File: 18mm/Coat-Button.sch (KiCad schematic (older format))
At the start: 25 parts, among them IC1 MADW__ATTINY13-MM, P1 CONN_1, P2 CONN_1, P3 CONN_1, P4 CONN_1

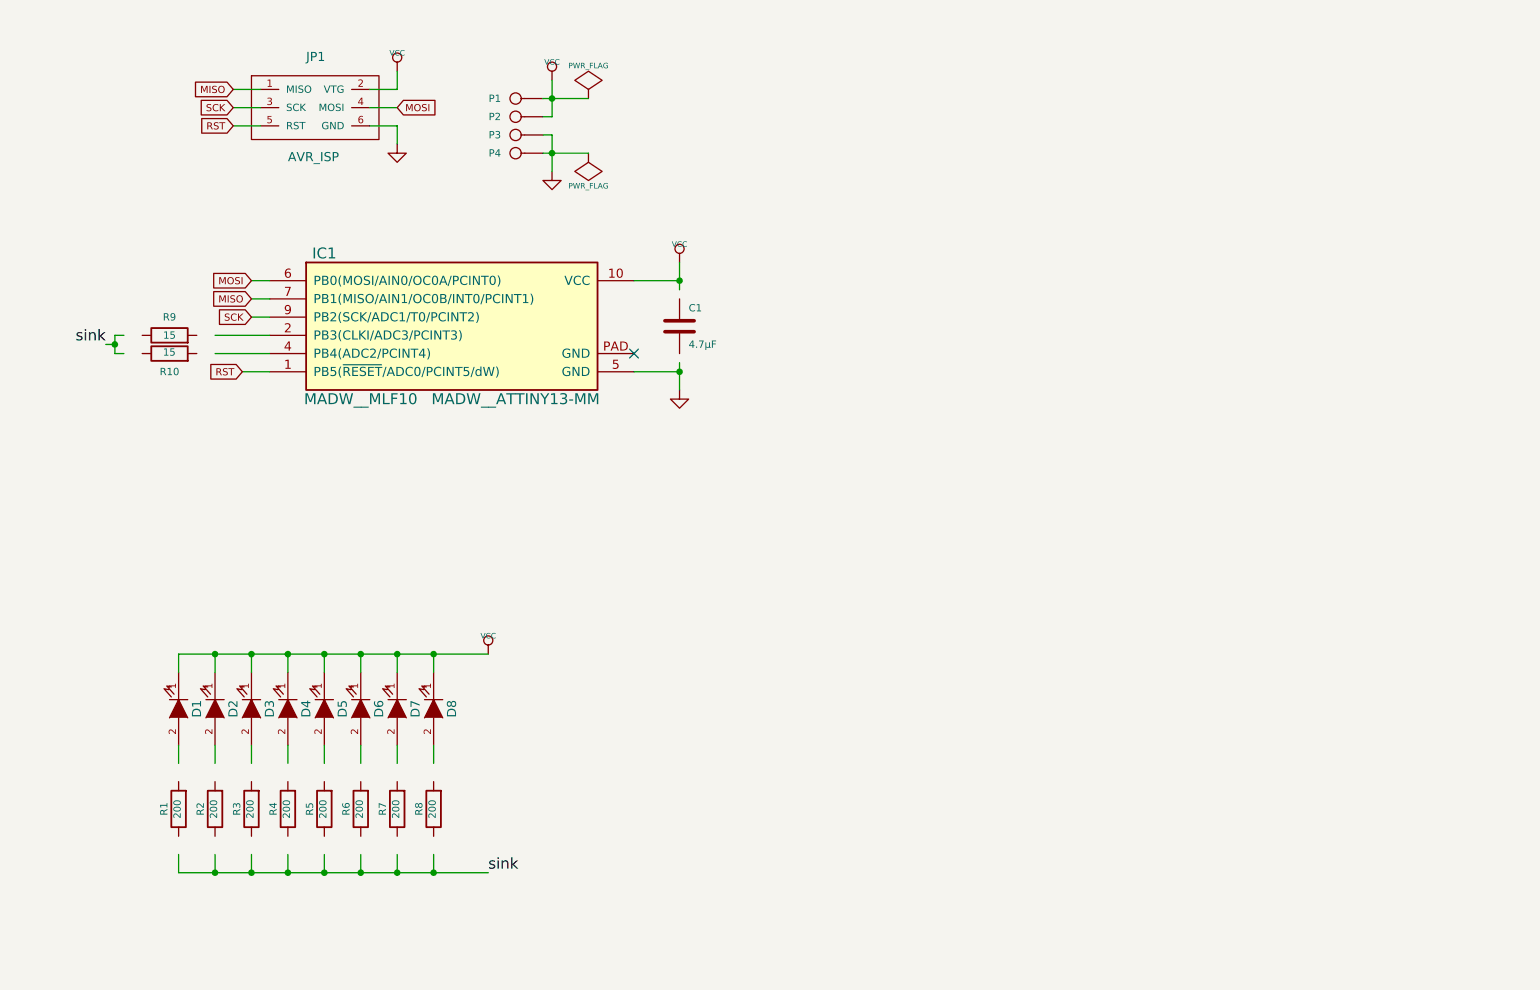
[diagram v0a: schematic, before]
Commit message: Made one with dual-colour LEDs (0805). Just to see if possible.
Had to use 0402 resitors...
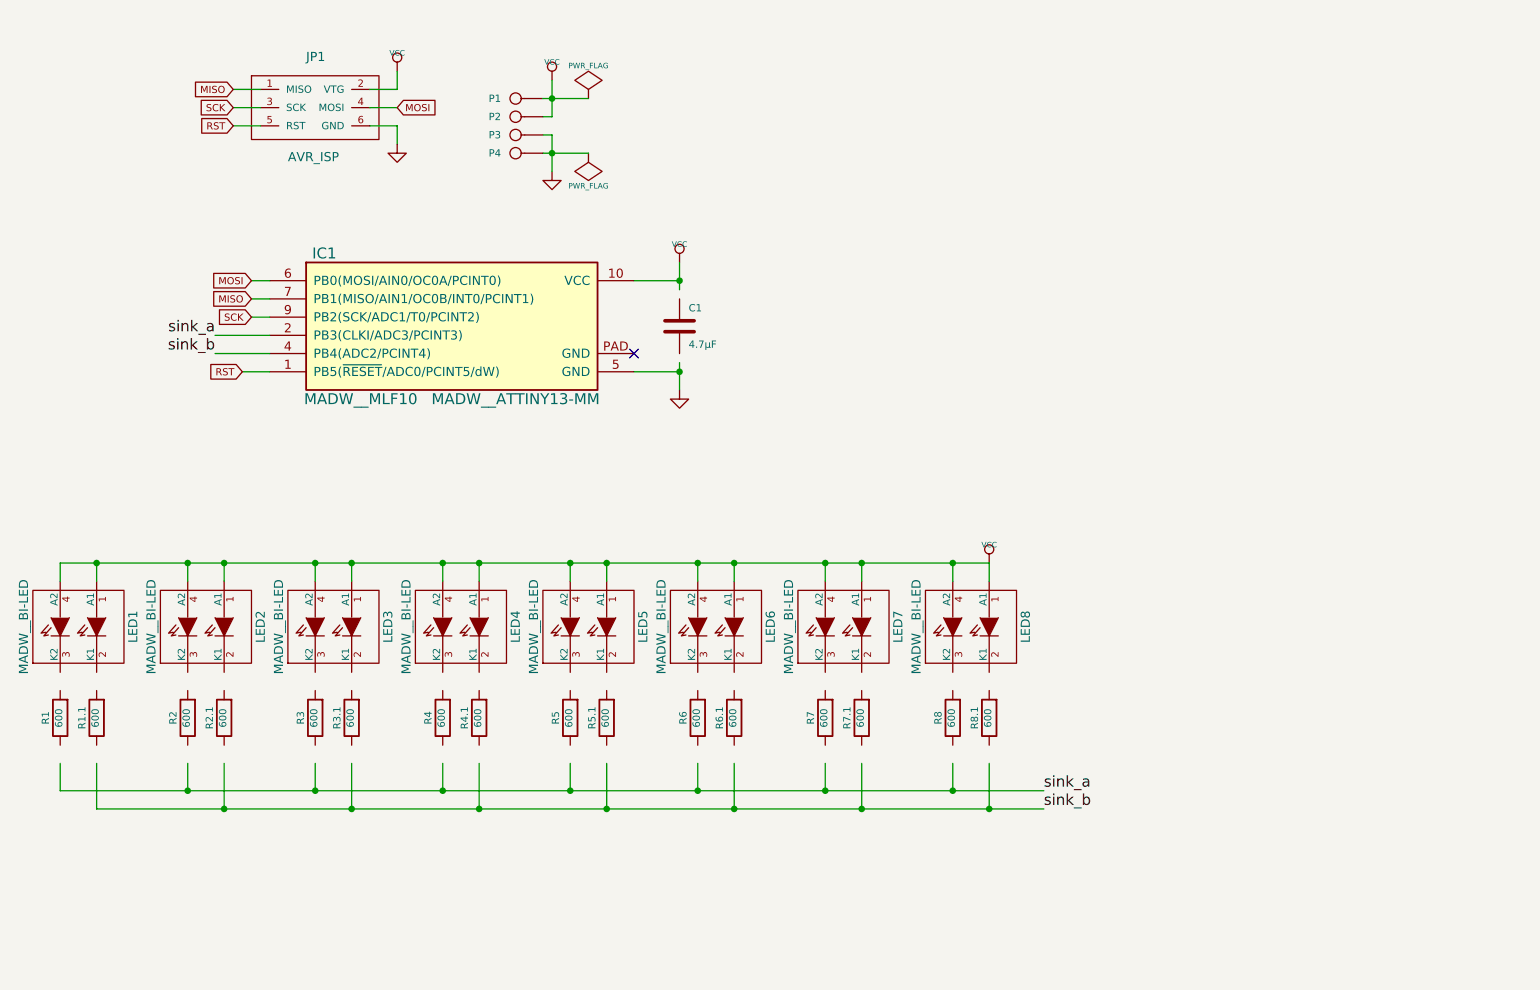
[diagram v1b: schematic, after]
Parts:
- removed D1, D2, D3, D4, D5, D6, D7, D8: LED, symbol LED
- removed R10, R9: 15, symbol R
- added LED1, LED2, LED3, LED4, LED5, LED6, LED7, LED8: MADW__BI-LED, symbol MADW__BI-LED
- added R1.1, R2.1, R3.1, R4.1, R5.1, R6.1, R7.1, R8.1: 600, symbol R
- R1, R2, R3, R4, R5, R6, R7, R8: value 200 -> 600
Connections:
- net labels added: sink_a, sink_b
- net labels removed: sink
- wire segments 54 -> 59
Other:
- moved on the sheet: R1, R2, R3, R4, R5, R6, R7, R8

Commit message: Added 2 SOT523 n-ch mosfets + reduced LED resistors.
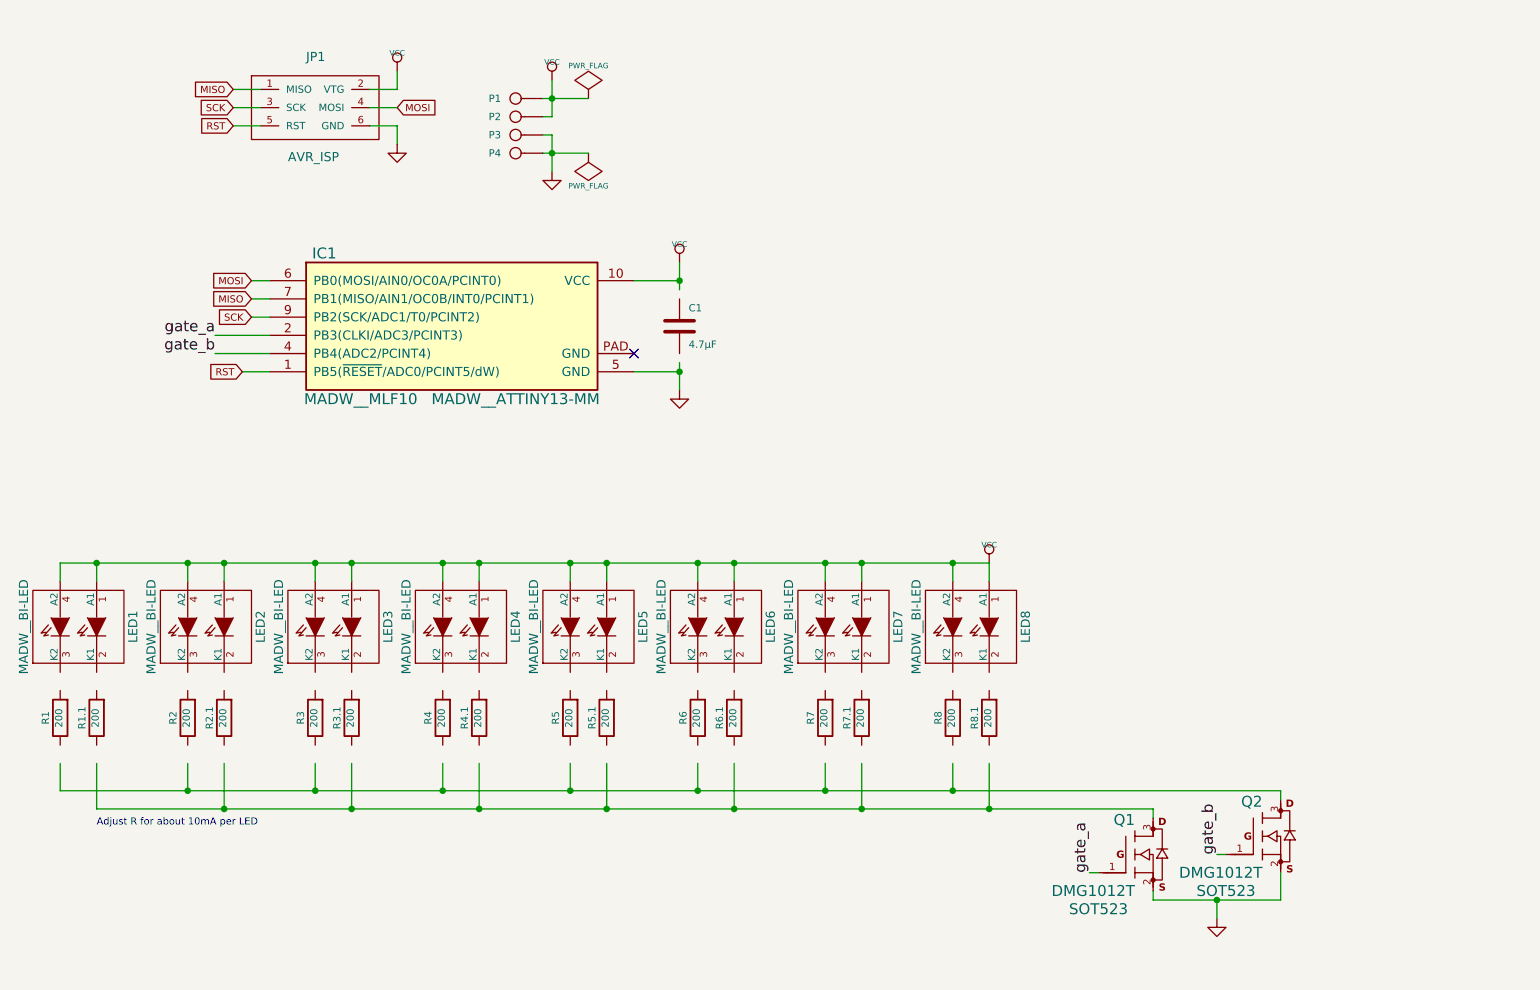
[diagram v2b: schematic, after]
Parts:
- added Q1, Q2: DMG1012T, SOT523, symbol MOSFET_N
- R1, R1.1, R2, R2.1, R3, R3.1, R4, R4.1, R5, R5.1, R6, R6.1, R7, R7.1, R8, R8.1: value 600 -> 200
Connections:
- net labels added: gate_a, gate_b
- net labels removed: sink_a, sink_b
- wire segments 59 -> 67
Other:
- note added: "Adjust R for about 10mA per LED"
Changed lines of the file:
@@
 EESchema Schematic File Version 2
+LIBS:my_parts
 LIBS:power
 LIBS:device
@@
 LIBS:contrib
 LIBS:valves
-LIBS:my_parts
 LIBS:Coat-Button-cache
 EELAYER 24 0
@@
 Sheet 1 1
 Title "Coat-Button"
-Date "23 Sep 2013"
-Rev "0.2"
+Date "25 Sep 2013"
+Rev "0.21"
 Comp "2013 - blog.spitzenpfeil.org"
 Comment1 ""
@@
 P 2300 5100
 F 0 "R1" V 2380 5100 40  0000 C CNN
-F 1 "600" V 2307 5101 40  0000 C CNN
+F 1 "200" V 2307 5101 40  0000 C CNN
 F 2 "" V 2230 5100 30  0000 C CNN
 F 3 "" H 2300 5100 30  0000 C CNN
@@
 P 3000 5100
 F 0 "R2" V 3080 5100 40  0000 C CNN
-F 1 "600" V 3007 5101 40  0000 C CNN
+F 1 "200" V 3007 5101 40  0000 C CNN
 F 2 "" V 2930 5100 30  0000 C CNN
 F 3 "" H 3000 5100 30  0000 C CNN
@@
 P 3700 5100
 F 0 "R3" V 3780 5100 40  0000 C CNN
-F 1 "600" V 3707 5101 40  0000 C CNN
+F 1 "200" V 3707 5101 40  0000 C CNN
 F 2 "" V 3630 5100 30  0000 C CNN
 F 3 "" H 3700 5100 30  0000 C CNN
@@
 P 4400 5100
 F 0 "R4" V 4480 5100 40  0000 C CNN
-F 1 "600" V 4407 5101 40  0000 C CNN
+F 1 "200" V 4407 5101 40  0000 C CNN
 F 2 "" V 4330 5100 30  0000 C CNN
 F 3 "" H 4400 5100 30  0000 C CNN
@@
 P 5100 5100
 F 0 "R5" V 5180 5100 40  0000 C CNN
-F 1 "600" V 5107 5101 40  0000 C CNN
+F 1 "200" V 5107 5101 40  0000 C CNN
 F 2 "" V 5030 5100 30  0000 C CNN
 F 3 "" H 5100 5100 30  0000 C CNN
@@
 P 5800 5100
 F 0 "R6" V 5880 5100 40  0000 C CNN
-F 1 "600" V 5807 5101 40  0000 C CNN
+F 1 "200" V 5807 5101 40  0000 C CNN
 F 2 "" V 5730 5100 30  0000 C CNN
 F 3 "" H 5800 5100 30  0000 C CNN
@@
 P 6500 5100
 F 0 "R7" V 6580 5100 40  0000 C CNN
-F 1 "600" V 6507 5101 40  0000 C CNN
+F 1 "200" V 6507 5101 40  0000 C CNN
 F 2 "" V 6430 5100 30  0000 C CNN
 F 3 "" H 6500 5100 30  0000 C CNN
@@
 P 7200 5100
 F 0 "R8" V 7280 5100 40  0000 C CNN
-F 1 "600" V 7207 5101 40  0000 C CNN
+F 1 "200" V 7207 5101 40  0000 C CNN
 F 2 "" V 7130 5100 30  0000 C CNN
 F 3 "" H 7200 5100 30  0000 C CNN
@@
 	3450 3100 3150 3100
 Text Label 3150 3000 2    60   ~ 0
-sink_a
-Text Label 7700 5500 0    60   ~ 0
-sink_a
+gate_a
 Wire Wire Line
 	4950 1900 5000 1900
@@
 P 2500 5100
 F 0 "R1.1" V 2580 5100 40  0000 C CNN
-F 1 "600" V 2507 5101 40  0000 C CNN
+F 1 "200" V 2507 5101 40  0000 C CNN
 F 2 "" V 2430 5100 30  0000 C CNN
 F 3 "" H 2500 5100 30  0000 C CNN
@@
 P 3200 5100
 F 0 "R2.1" V 3280 5100 40  0000 C CNN
-F 1 "600" V 3207 5101 40  0000 C CNN
+F 1 "200" V 3207 5101 40  0000 C CNN
 F 2 "" V 3130 5100 30  0000 C CNN
 F 3 "" H 3200 5100 30  0000 C CNN
@@
 P 3900 5100
 F 0 "R3.1" V 3980 5100 40  0000 C CNN
-F 1 "600" V 3907 5101 40  0000 C CNN
+F 1 "200" V 3907 5101 40  0000 C CNN
 F 2 "" V 3830 5100 30  0000 C CNN
 F 3 "" H 3900 5100 30  0000 C CNN
@@
 P 4600 5100
 F 0 "R4.1" V 4680 5100 40  0000 C CNN
-F 1 "600" V 4607 5101 40  0000 C CNN
+F 1 "200" V 4607 5101 40  0000 C CNN
 F 2 "" V 4530 5100 30  0000 C CNN
 F 3 "" H 4600 5100 30  0000 C CNN
@@
 P 5300 5100
 F 0 "R5.1" V 5380 5100 40  0000 C CNN
-F 1 "600" V 5307 5101 40  0000 C CNN
+F 1 "200" V 5307 5101 40  0000 C CNN
 F 2 "" V 5230 5100 30  0000 C CNN
 F 3 "" H 5300 5100 30  0000 C CNN
@@
 P 6000 5100
 F 0 "R6.1" V 6080 5100 40  0000 C CNN
-F 1 "600" V 6007 5101 40  0000 C CNN
+F 1 "200" V 6007 5101 40  0000 C CNN
 F 2 "" V 5930 5100 30  0000 C CNN
 F 3 "" H 6000 5100 30  0000 C CNN
@@
 P 6700 5100
 F 0 "R7.1" V 6780 5100 40  0000 C CNN
-F 1 "600" V 6707 5101 40  0000 C CNN
+F 1 "200" V 6707 5101 40  0000 C CNN
 F 2 "" V 6630 5100 30  0000 C CNN
 F 3 "" H 6700 5100 30  0000 C CNN
@@
 P 7400 5100
 F 0 "R8.1" V 7480 5100 40  0000 C CNN
-F 1 "600" V 7407 5101 40  0000 C CNN
+F 1 "200" V 7407 5101 40  0000 C CNN
 F 2 "" V 7330 5100 30  0000 C CNN
 F 3 "" H 7400 5100 30  0000 C CNN
@@
 	2300 5350 2300 5500
 Wire Wire Line
-	2300 5500 7700 5500
-Wire Wire Line
 	3000 5500 3000 5350
 Wire Wire Line
@@
 	2500 5350 2500 5600
 Wire Wire Line
-	2500 5600 7700 5600
+	2500 5600 8300 5600
 Wire Wire Line
 	3200 5600 3200 5350
@@
 	5300 5350 5300 5600
 Connection ~ 5300 5600
-Text Label 7700 5600 0    60   ~ 0
-sink_b
 Connection ~ 7200 5500
 Connection ~ 7400 5600
 Text Label 3150 3100 2    60   ~ 0
-sink_b
+gate_b
+$Comp
+L MOSFET_N Q1
+U 1 1 5242F7C2
+P 8000 5950
+F 0 "Q1" H 8200 6240 60  0000 R CNN
+F 1 "DMG1012T" H 8200 5850 60  0000 R CNN
+F 2 "SOT523" H 8000 5750 60  0000 C CNN
+F 3 "" H 8000 5950 60  0000 C CNN
+	1    8000 5950
+	1    0    0    -1
+$EndComp
+$Comp
+L MOSFET_N Q2
+U 1 1 5242F7D6
+P 8700 5850
+F 0 "Q2" H 8900 6140 60  0000 R CNN
+F 1 "DMG1012T" H 8900 5750 60  0000 R CNN
+F 2 "SOT523" H 8700 5650 60  0000 C CNN
+F 3 "" H 8700 5850 60  0000 C CNN
+	1    8700 5850
+	1    0    0    -1
+$EndComp
+Wire Wire Line
+	8300 6100 9000 6100
+Wire Wire Line
+	9000 6100 9000 5950
+Wire Wire Line
+	8650 6100 8650 6200
+Connection ~ 8650 6100
+$Comp
+L GND #PWR010
+U 1 1 5242F8C4
+P 8650 6200
+F 0 "#PWR010" H 8650 6200 30  0001 C CNN
+F 1 "GND" H 8650 6130 30  0001 C CNN
+F 2 "" H 8650 6200 60  0000 C CNN
+F 3 "" H 8650 6200 60  0000 C CNN
+	1    8650 6200
+	1    0    0    -1
+$EndComp
+Wire Wire Line
+	2300 5500 9000 5500
+Wire Wire Line
+	9000 5500 9000 5550
+Wire Wire Line
+	8300 5600 8300 5650
+Wire Wire Line
+	8300 6050 8300 6100
+Text Label 7950 5950 1    60   ~ 0
+gate_a
+Text Label 8650 5850 1    60   ~ 0
+gate_b
+Wire Wire Line
+	8650 5850 8700 5850
+Wire Wire Line
+	7950 5950 8000 5950
+Text Notes 2500 5700 0    39   ~ 0
+Adjust R for about 10mA per LED
 $EndSCHEMATC

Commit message: Added alternative 0603 R. footprints for single-color mode.
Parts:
- added R1.2, R2.2, R3.2, R4.2, R5.2, R6.2, R7.2, R8.2: 200, symbol R
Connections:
- wire segments 67 -> 83
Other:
- note added: "(*)"
- note added: "* Adjust R for about 10mA per LED\n\n(*) Rx.2 alternate footprint for single-color LED. Use instead of Rx and Rx.1"
- note removed: "Adjust R for about 10mA per LED"
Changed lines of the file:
@@
 Sheet 1 1
 Title "Coat-Button"
-Date "25 Sep 2013"
-Rev "0.21"
+Date "03 Oct 2013"
+Rev "0.22"
 Comp "2013 - blog.spitzenpfeil.org"
 Comment1 ""
@@
 	7950 5950 8000 5950
 Text Notes 2500 5700 0    39   ~ 0
-Adjust R for about 10mA per LED
+* Adjust R for about 10mA per LED\n\n(*) Rx.2 alternate footprint for single-color LED. Use instead of Rx and Rx.1
+$Comp
+L R R1.2
+U 1 1 524DA6D3
+P 2600 5100
+F 0 "R1.2" V 2680 5100 40  0000 C CNN
+F 1 "200" V 2607 5101 40  0000 C CNN
+F 2 "" V 2530 5100 30  0000 C CNN
+F 3 "" H 2600 5100 30  0000 C CNN
+	1    2600 5100
+	1    0    0    -1
+$EndComp
+$Comp
+L R R2.2
+U 1 1 524DA6E7
+P 3300 5100
+F 0 "R2.2" V 3380 5100 40  0000 C CNN
+F 1 "200" V 3307 5101 40  0000 C CNN
+F 2 "" V 3230 5100 30  0000 C CNN
+F 3 "" H 3300 5100 30  0000 C CNN
+	1    3300 5100
+	1    0    0    -1
+$EndComp
+$Comp
+L R R3.2
+U 1 1 524DA6F9
+P 4000 5100
+F 0 "R3.2" V 4080 5100 40  0000 C CNN
+F 1 "200" V 4007 5101 40  0000 C CNN
+F 2 "" V 3930 5100 30  0000 C CNN
+F 3 "" H 4000 5100 30  0000 C CNN
+	1    4000 5100
+	1    0    0    -1
+$EndComp
+$Comp
+L R R4.2
+U 1 1 524DA704
+P 4700 5100
+F 0 "R4.2" V 4780 5100 40  0000 C CNN
+F 1 "200" V 4707 5101 40  0000 C CNN
+F 2 "" V 4630 5100 30  0000 C CNN
+F 3 "" H 4700 5100 30  0000 C CNN
+	1    4700 5100
+	1    0    0    -1
+$EndComp
+$Comp
+L R R5.2
+U 1 1 524DA70F
+P 5400 5100
+F 0 "R5.2" V 5480 5100 40  0000 C CNN
+F 1 "200" V 5407 5101 40  0000 C CNN
+F 2 "" V 5330 5100 30  0000 C CNN
+F 3 "" H 5400 5100 30  0000 C CNN
+	1    5400 5100
+	1    0    0    -1
+$EndComp
+$Comp
+L R R6.2
+U 1 1 524DA71A
+P 6100 5100
+F 0 "R6.2" V 6180 5100 40  0000 C CNN
+F 1 "200" V 6107 5101 40  0000 C CNN
+F 2 "" V 6030 5100 30  0000 C CNN
+F 3 "" H 6100 5100 30  0000 C CNN
+	1    6100 5100
+	1    0    0    -1
+$EndComp
+$Comp
+L R R7.2
+U 1 1 524DA725
+P 6800 5100
+F 0 "R7.2" V 6880 5100 40  0000 C CNN
+F 1 "200" V 6807 5101 40  0000 C CNN
+F 2 "" V 6730 5100 30  0000 C CNN
+F 3 "" H 6800 5100 30  0000 C CNN
+	1    6800 5100
+	1    0    0    -1
+$EndComp
+$Comp
+L R R8.2
+U 1 1 524DA730
+P 7500 5100
+F 0 "R8.2" V 7580 5100 40  0000 C CNN
+F 1 "200" V 7507 5101 40  0000 C CNN
+F 2 "" V 7430 5100 30  0000 C CNN
+F 3 "" H 7500 5100 30  0000 C CNN
+	1    7500 5100
+	1    0    0    -1
+$EndComp
+Wire Wire Line
+	2500 4850 2600 4850
+Wire Wire Line
+	2500 5350 2600 5350
+Wire Wire Line
+	3200 5350 3300 5350
+Wire Wire Line
+	3200 4850 3300 4850
+Wire Wire Line
+	3900 4850 4000 4850
+Wire Wire Line
+	3900 5350 4000 5350
+Text Notes 2650 5000 0    39   ~ 0
+(*)
+Wire Wire Line
+	4600 4850 4700 4850
+Wire Wire Line
+	5300 4850 5400 4850
+Wire Wire Line
+	6000 4850 6100 4850
+Wire Wire Line
+	4600 5350 4700 5350
+Wire Wire Line
+	5300 5350 5400 5350
+Wire Wire Line
+	6000 5350 6100 5350
+Wire Wire Line
+	6700 4850 6800 4850
+Wire Wire Line
+	6700 5350 6800 5350
+Wire Wire Line
+	7400 4850 7500 4850
+Wire Wire Line
+	7400 5350 7500 5350
 $EndSCHEMATC
